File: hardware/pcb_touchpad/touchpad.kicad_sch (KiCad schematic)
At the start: 24 parts, among them U1 IQS9151

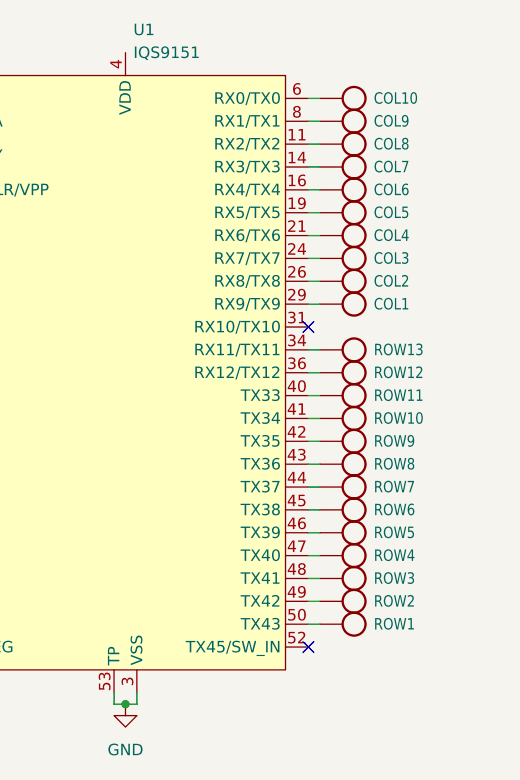
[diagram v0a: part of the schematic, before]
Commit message: assigned correct nets to vias
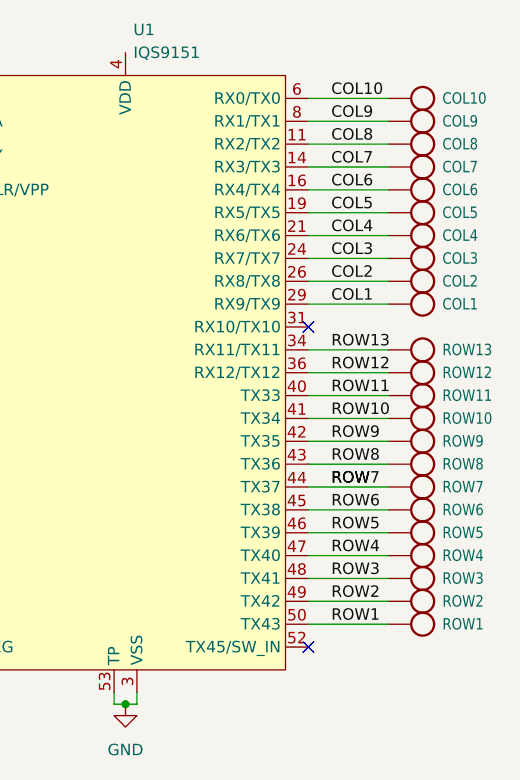
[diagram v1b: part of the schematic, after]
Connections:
- net ROW: now reaches ROW7.P1, U1.44 (TX37)
- net COL10: now reaches COL10.P1, U1.6 (RX0/TX0)
- net ROW2: now reaches ROW2.P1, U1.49 (TX42)
- net ROW11: now reaches ROW11.P1, U1.40 (TX33)
- net COL9: now reaches COL9.P1, U1.8 (RX1/TX1)
- net COL3: now reaches COL3.P1, U1.24 (RX7/TX7)
- net COL5: now reaches COL5.P1, U1.19 (RX5/TX5)
- net ROW8: now reaches ROW8.P1, U1.43 (TX36)
- net ROW6: now reaches ROW6.P1, U1.45 (TX38)
- net COL8: now reaches COL8.P1, U1.11 (RX2/TX2)
- net ROW10: now reaches ROW10.P1, U1.41 (TX34)
- net COL7: now reaches COL7.P1, U1.14 (RX3/TX3)
- net ROW1: now reaches ROW1.P1, U1.50 (TX43)
- net ROW9: now reaches ROW9.P1, U1.42 (TX35)
- net COL4: now reaches COL4.P1, U1.21 (RX6/TX6)
- net ROW13: now reaches ROW13.P1, U1.34 (RX11/TX11)
- net ROW3: now reaches ROW3.P1, U1.48 (TX41)
- net ROW5: now reaches ROW5.P1, U1.46 (TX39)
- net ROW12: now reaches ROW12.P1, U1.36 (RX12/TX12)
- net ROW4: now reaches ROW4.P1, U1.47 (TX40)
- net COL1: now reaches COL1.P1, U1.29 (RX9/TX9)
- net COL2: now reaches COL2.P1, U1.26 (RX8/TX8)
- net COL6: now reaches COL6.P1, U1.16 (RX4/TX4)
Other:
- moved on the sheet: COL1, COL10, COL2, COL3, COL4, COL5, COL6, COL7, COL8, COL9, ROW1, ROW10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

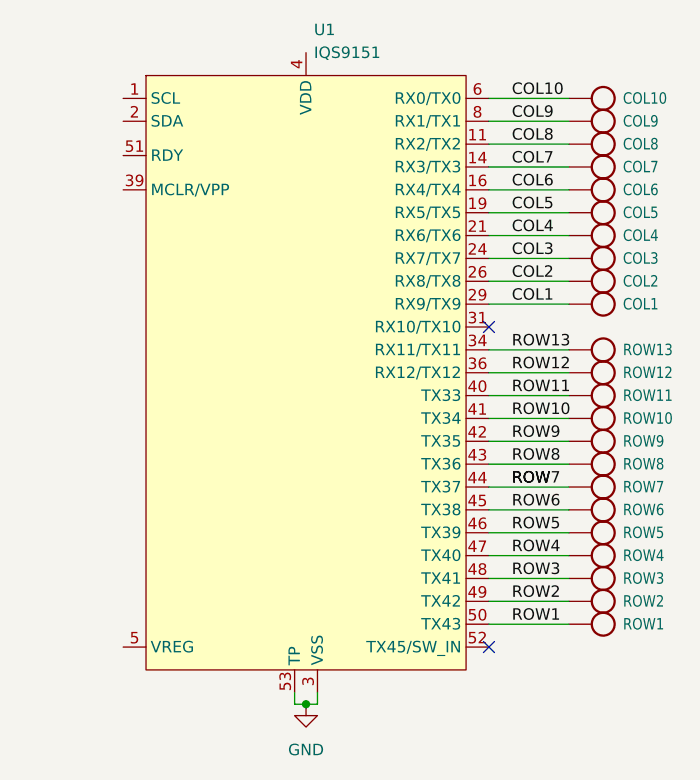
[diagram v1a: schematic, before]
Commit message: touchpad: regenerated touchpad, made IQS7211E symbol
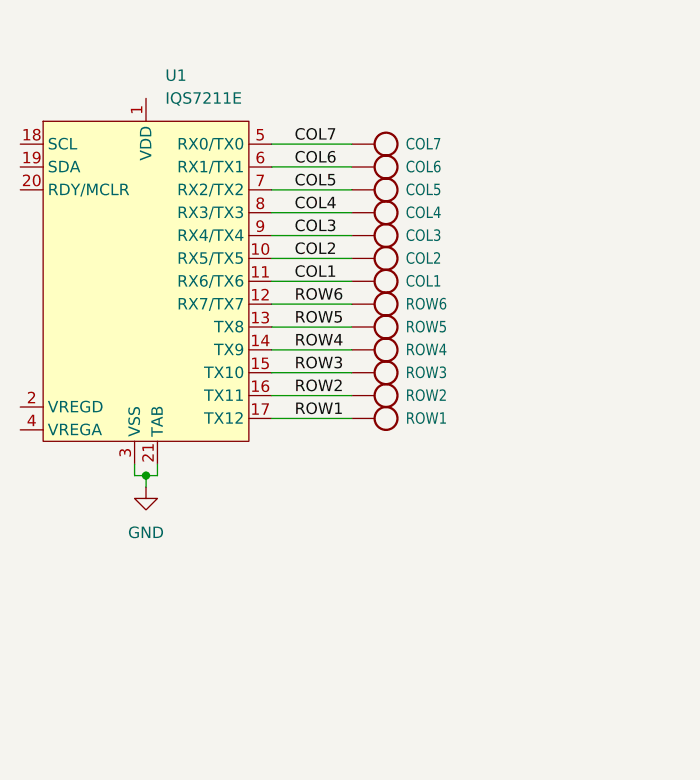
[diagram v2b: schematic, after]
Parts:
- removed COL10, COL8, COL9, ROW10, ROW11, ROW12, ROW13, ROW7, ROW8, ROW9: TESTPOINTPAD_0_5MM, Touchpad:PAD_0_5MM, symbol Touchpad-eagle-import:TESTPOINTPAD_0_5MM
- removed U1: IQS9151, Package_DFN_QFN:VQFN-52-1EP_6x6mm_P0.4mm_EP4.7x4.7mm, symbol IQS9151:IQS9151
- added U1: IQS7211E, Package_DFN_QFN:QFN-20-1EP_3x3mm_P0.4mm_EP1.65x1.65mm, symbol IQS:IQS7211E
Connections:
- net COL1: now also U1.11 (RX6/TX6)
- net COL2: now also U1.10 (RX5/TX5)
- net COL3: now also U1.9 (RX4/TX4)
- net COL4: now also U1.8 (RX3/TX3)
- net COL5: now also U1.7 (RX2/TX2)
- net COL6: now also U1.6 (RX1/TX1)
- net COL7: now also U1.5 (RX0/TX0)
- net GND: now also U1.21 (TAB), U1.3 (VSS)
- net ROW1: now also U1.17 (TX12)
- net ROW2: now also U1.16 (TX11)
- net ROW3: now also U1.15 (TX10)
- net ROW4: now also U1.14 (TX9)
- net ROW5: now also U1.13 (TX8)
- net ROW6: now also U1.12 (RX7/TX7)
- no-connect marks 2 -> 0
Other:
- moved on the sheet: COL1, COL2, COL3, COL4, COL5, COL6, COL7, ROW1, ROW2, ROW3, ROW4, ROW5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

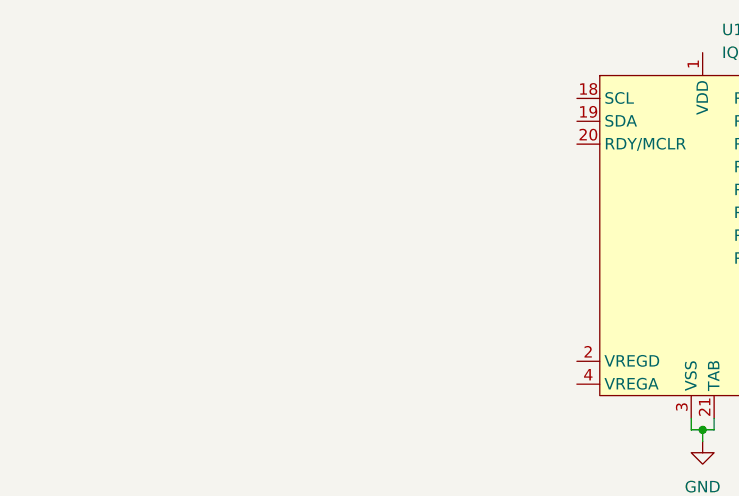
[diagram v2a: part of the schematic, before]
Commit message: added conn to trackpad pcb, updated mockup, placed conn
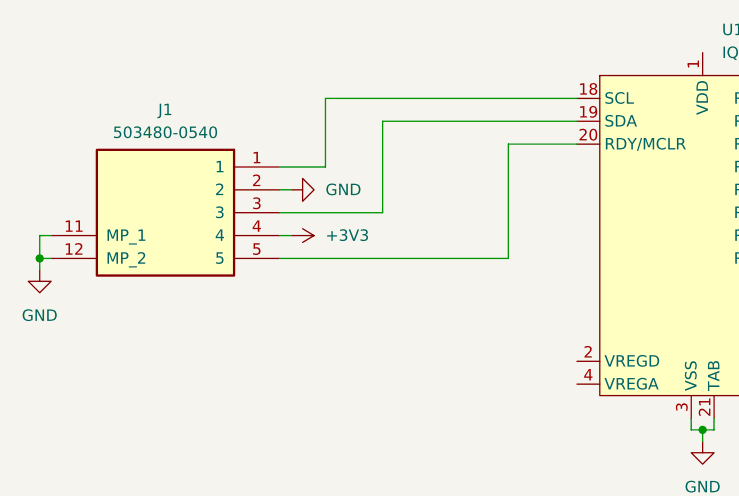
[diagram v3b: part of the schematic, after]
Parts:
- added J1: 503480-0540, 5034800540:503480-0540, symbol 503480-0540:503480-0540
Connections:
- net GND: now also J1.11 (MP_1), J1.12 (MP_2), J1.2
- net at U1.18 (SCL): now also J1.1
- net at U1.19 (SDA): now also J1.3
- net at U1.20 (RDY/MCLR): now also J1.5
- new net +3V3: J1.4

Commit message: small stuff
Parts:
- added C1, C2, C3: 1u, Capacitor_SMD:C_0402_1005Metric, symbol Device:C_Small
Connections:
- net +3V3: now also J1.5, U1.1 (VDD), C3.1; no longer J1.4
- net GND: now also C1.2, C2.2, C3.2
- net at U1.20 (RDY/MCLR): now also J1.4; no longer J1.5
- net at U1.2 (VREGD): now also C2.1
- net at U1.4 (VREGA): now also C1.1

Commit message: first touchpad draft
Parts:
- J1: footprint 5034800540:503480-0540 -> 503480-0540:503480-0540
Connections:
- net GND: now also J1.MP_1, J1.MP_2; no longer J1.11 (MP_1), J1.12 (MP_2)
- net ROW1: now also U1.12 (RX7/TX7); no longer U1.17 (TX12)
- net ROW2: now also U1.13 (TX8); no longer U1.16 (TX11)
- net ROW3: now also U1.14 (TX9); no longer U1.15 (TX10)
- net ROW4: now also U1.15 (TX10); no longer U1.14 (TX9)
- net ROW5: now also U1.16 (TX11); no longer U1.13 (TX8)
- net ROW6: now also U1.17 (TX12); no longer U1.12 (RX7/TX7)
- net SCL: now reaches J1.1, U1.18 (SCL)
- net SDA: now reaches J1.3, U1.19 (SDA)
- net RDY/MCLR: now reaches J1.4, U1.20 (RDY/MCLR)
- net VREGD: now reaches C2.1, U1.2 (VREGD)
- net VREGA: now reaches C1.1, U1.4 (VREGA)
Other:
- moved on the sheet: C1, C2, ROW1, ROW2, ROW3, ROW4, ROW5, ROW6

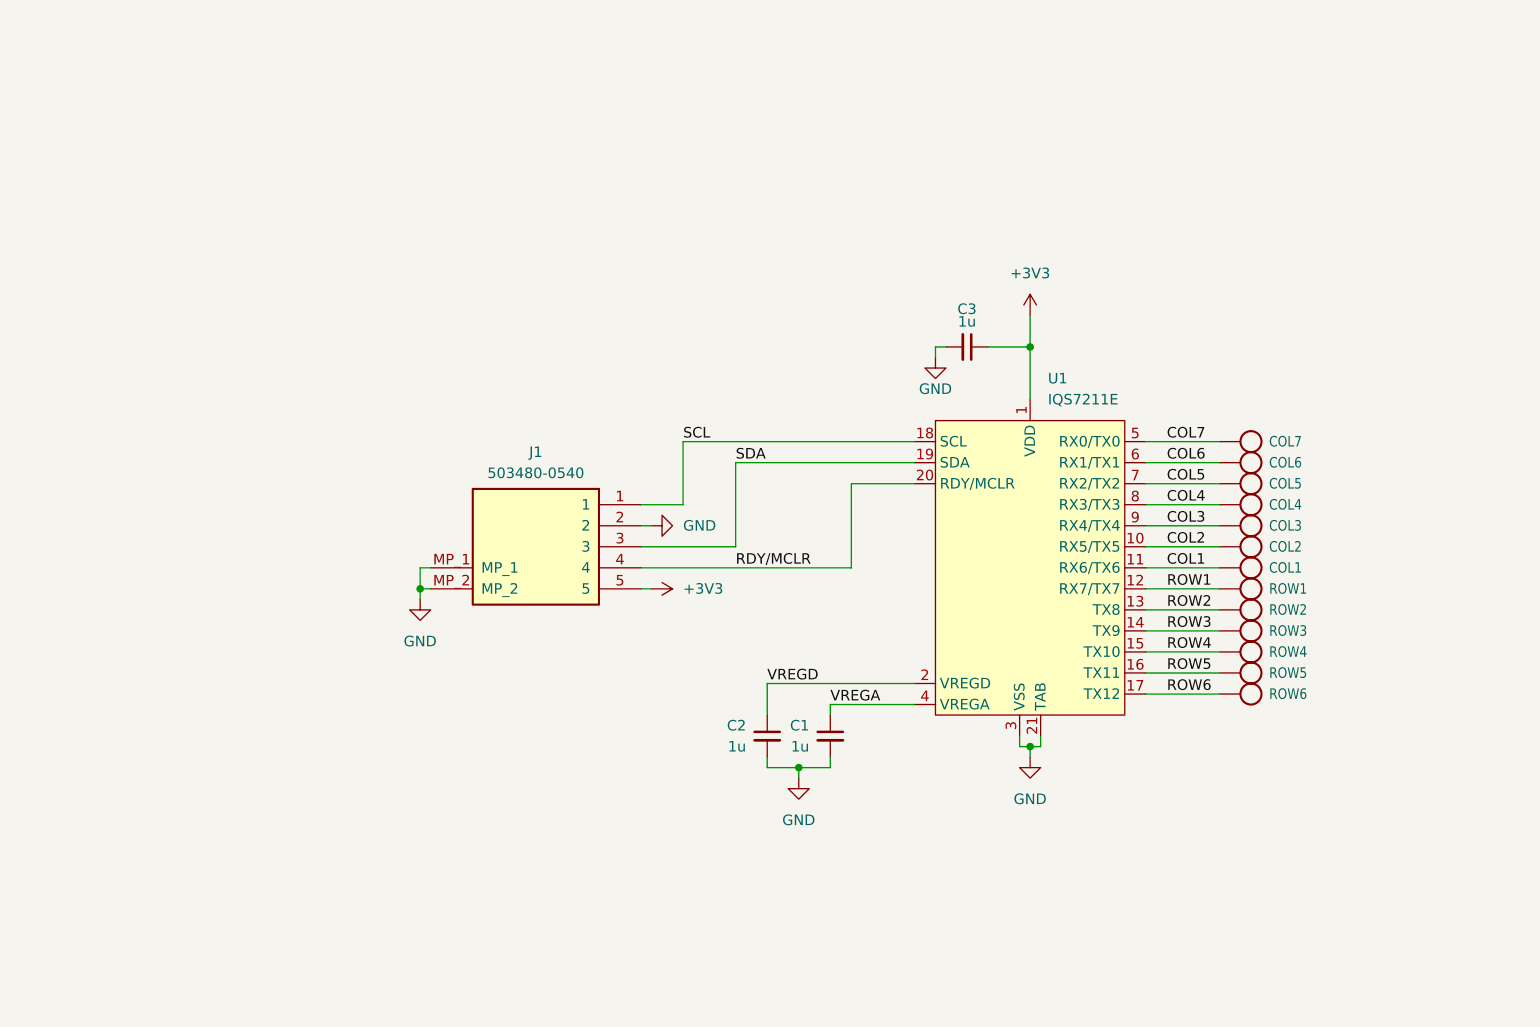
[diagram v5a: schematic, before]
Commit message: added touchpad silkscreen
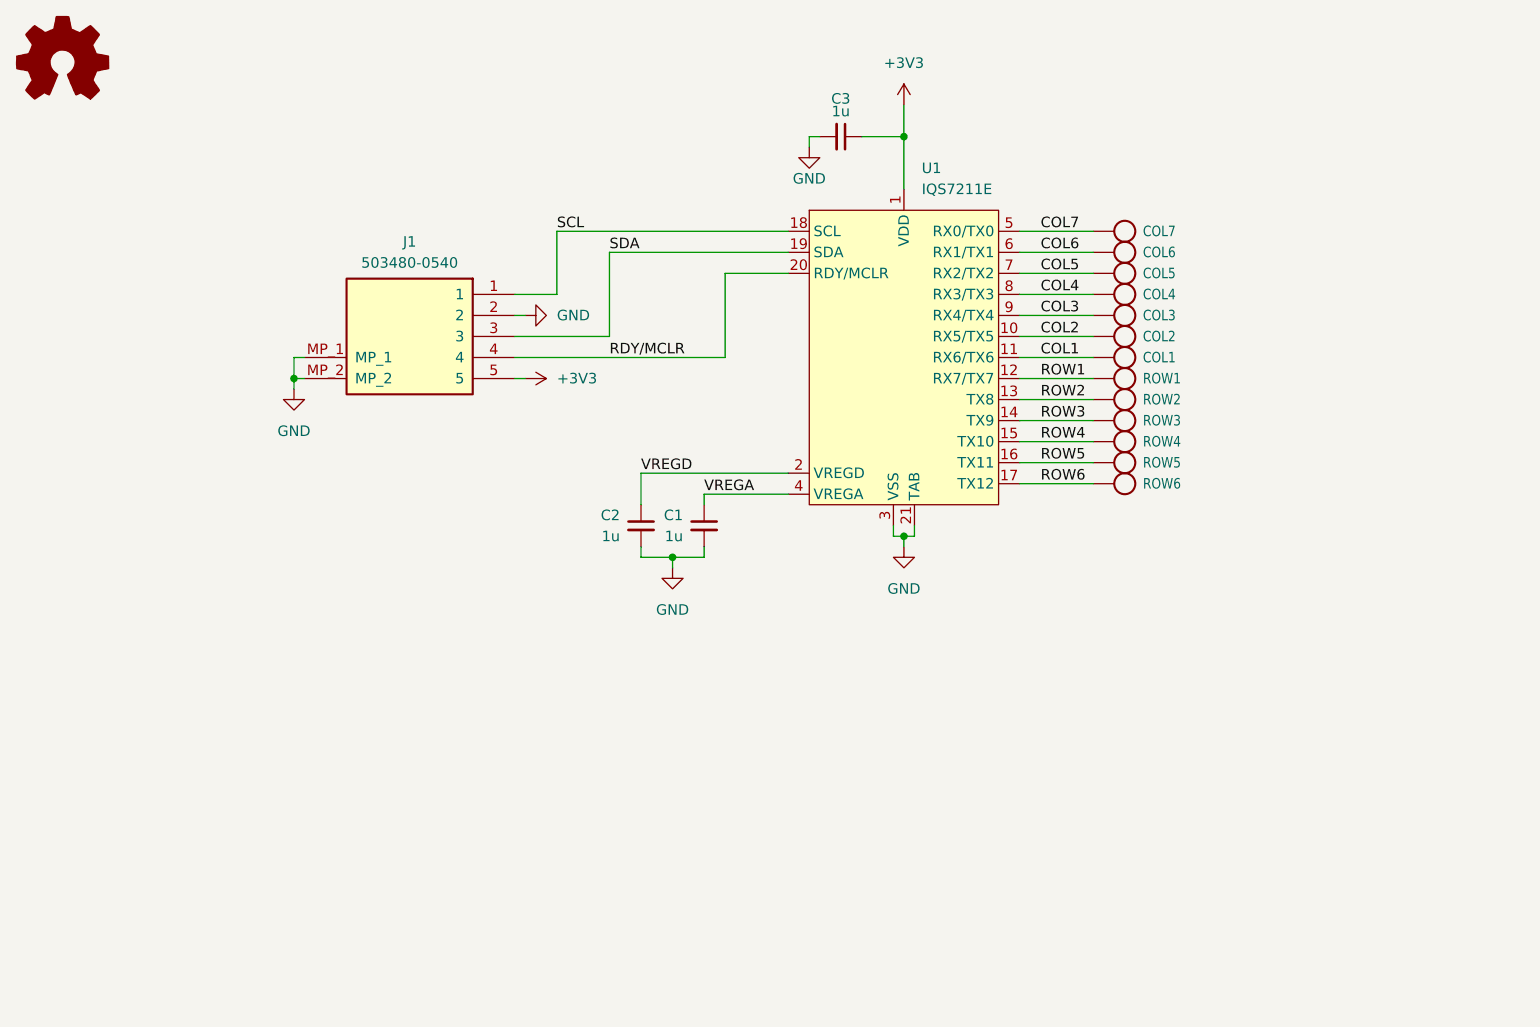
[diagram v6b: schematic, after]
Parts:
- added SYM1: Logo_Open_Hardware_Small, Symbol:OSHW-Logo2_14.6x12mm_SilkScreen, symbol Graphic:Logo_Open_Hardware_Small
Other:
- company: (none) -> gensis
- title: (none) -> Touchpad
- moved on the sheet: C1, C2, C3, COL1, COL2, COL3, COL4, COL5, COL6, COL7, J1, ROW1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
